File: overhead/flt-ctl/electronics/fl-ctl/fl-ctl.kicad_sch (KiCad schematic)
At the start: 29 parts, among them J1 Conn_02x01, J2 Conn_02x05_Counter_Clockwise

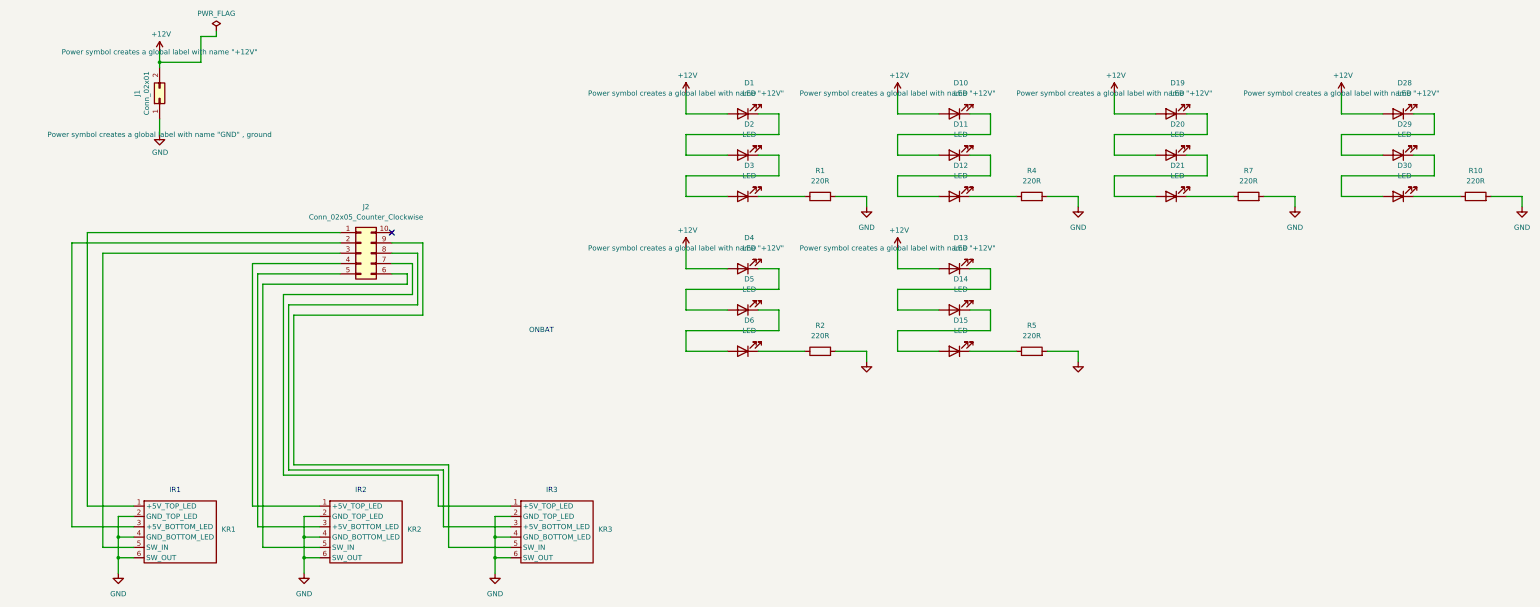
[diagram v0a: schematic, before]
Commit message: Finalised ROuting for FLT-CTL CPT Side, and cleaned up ADIRS Panel PCB
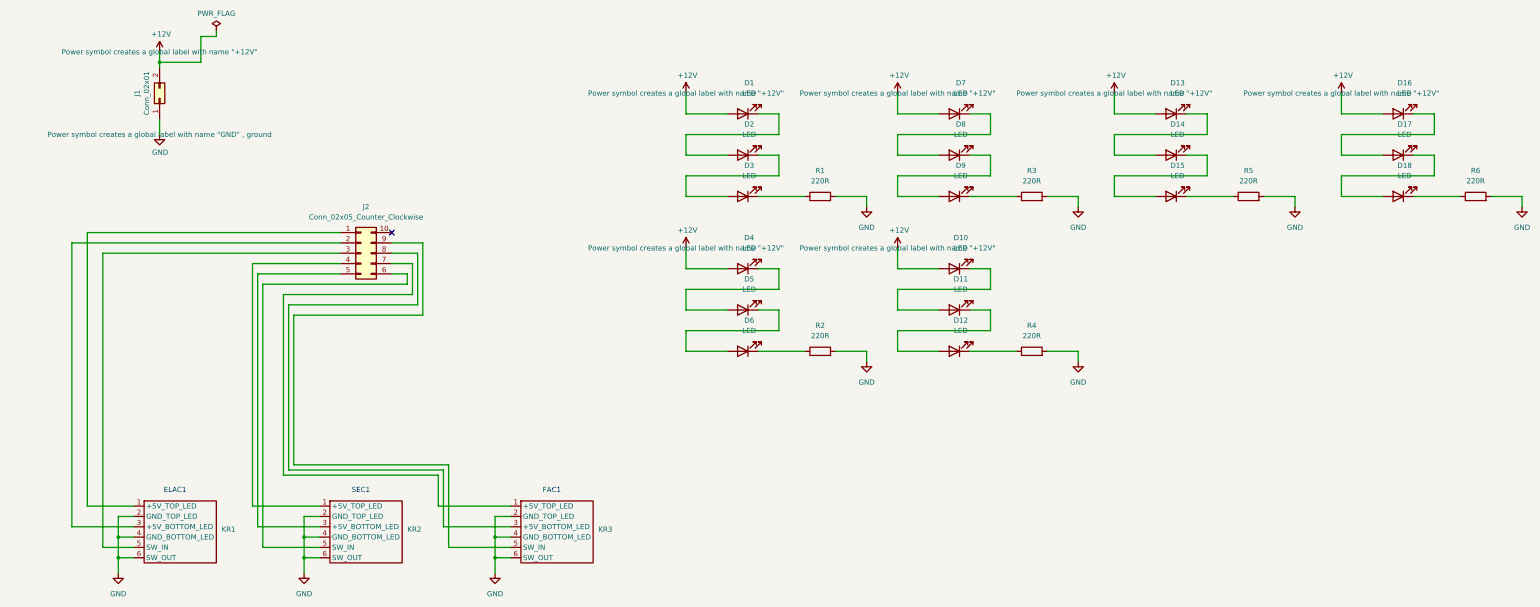
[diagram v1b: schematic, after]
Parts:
- renumbered D13 to D10, D14 to D11, D15 to D12, D19 to D13, D20 to D14, D21 to D15, D28 to D16, D29 to D17, D30 to D18, D10 to D7, D11 to D8, D12 to D9, R4 to R3, R5 to R4, R7 to R5, R10 to R6
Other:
- note added: "ELAC1"
- note added: "FAC1"
- note added: "SEC1"
- note removed: "IR1"
- note removed: "IR2"
- note removed: "IR3"
- note removed: "ONBAT"

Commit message: Updated all LEDs for SMD!
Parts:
- D1, D10, D11, D12, D13, D14, D15, D16, D17, D18, D2, D3, D4, D5, D6, D7, D8, D9: footprint LED_THT:LED_D5.0mm_Clear -> OpenA3XX:LED_Everlight-SMD3528_3.5x2.8mm_67-21ST
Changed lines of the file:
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@@
 			)
 		)
-		(property "Footprint" "LED_THT:LED_D5.0mm_Clear"
+		(property "Footprint" "OpenA3XX:LED_Everlight-SMD3528_3.5x2.8mm_67-21ST"
 			(at 187.96 90.17 0)
 			(effects
@@
 			)
 		)
-		(property "Footprint" "LED_THT:LED_D5.0mm_Clear"
+		(property "Footprint" "OpenA3XX:LED_Everlight-SMD3528_3.5x2.8mm_67-21ST"
 			(at 349.25 62.23 0)
 			(effects
@@
 			)
 		)
-		(property "Footprint" "LED_THT:LED_D5.0mm_Clear"
+		(property "Footprint" "OpenA3XX:LED_Everlight-SMD3528_3.5x2.8mm_67-21ST"
 			(at 187.96 100.33 0)
 			(effects
@@
 			)
 		)
-		(property "Footprint" "LED_THT:LED_D5.0mm_Clear"
+		(property "Footprint" "OpenA3XX:LED_Everlight-SMD3528_3.5x2.8mm_67-21ST"
 			(at 293.37 52.07 0)
 			(effects
@@
 			)
 		)
-		(property "Footprint" "LED_THT:LED_D5.0mm_Clear"
+		(property "Footprint" "OpenA3XX:LED_Everlight-SMD3528_3.5x2.8mm_67-21ST"
 			(at 349.25 52.07 0)
 			(effects
@@
 			)
 		)
-		(property "Footprint" "LED_THT:LED_D5.0mm_Clear"
+		(property "Footprint" "OpenA3XX:LED_Everlight-SMD3528_3.5x2.8mm_67-21ST"
 			(at 293.37 62.23 0)
 			(effects
@@
 			)
 		)
-		(property "Footprint" "LED_THT:LED_D5.0mm_Clear"
+		(property "Footprint" "OpenA3XX:LED_Everlight-SMD3528_3.5x2.8mm_67-21ST"
 			(at 240.03 41.91 0)
 			(effects
@@
 			)
 		)
-		(property "Footprint" "LED_THT:LED_D5.0mm_Clear"
+		(property "Footprint" "OpenA3XX:LED_Everlight-SMD3528_3.5x2.8mm_67-21ST"
 			(at 240.03 62.23 0)
 			(effects
@@
 			)
 		)
-		(property "Footprint" "LED_THT:LED_D5.0mm_Clear"
+		(property "Footprint" "OpenA3XX:LED_Everlight-SMD3528_3.5x2.8mm_67-21ST"
 			(at 349.25 41.91 0)
 			(effects
@@
 			)
 		)
-		(property "Footprint" "LED_THT:LED_D5.0mm_Clear"
+		(property "Footprint" "OpenA3XX:LED_Everlight-SMD3528_3.5x2.8mm_67-21ST"
 			(at 293.37 41.91 0)
 			(effects
@@
 			)
 		)
-		(property "Footprint" "LED_THT:LED_D5.0mm_Clear"
+		(property "Footprint" "OpenA3XX:LED_Everlight-SMD3528_3.5x2.8mm_67-21ST"
 			(at 187.96 41.91 0)
 			(effects
@@
 			)
 		)
-		(property "Footprint" "LED_THT:LED_D5.0mm_Clear"
+		(property "Footprint" "OpenA3XX:LED_Everlight-SMD3528_3.5x2.8mm_67-21ST"
 			(at 187.96 52.07 0)
 			(effects
@@
 			)
 		)
-		(property "Footprint" "LED_THT:LED_D5.0mm_Clear"
+		(property "Footprint" "OpenA3XX:LED_Everlight-SMD3528_3.5x2.8mm_67-21ST"
 			(at 187.96 80.01 0)
 			(effects
@@
 			)
 		)
-		(property "Footprint" "LED_THT:LED_D5.0mm_Clear"
+		(property "Footprint" "OpenA3XX:LED_Everlight-SMD3528_3.5x2.8mm_67-21ST"
 			(at 240.03 90.17 0)
 			(effects
@@
 			)
 		)
-		(property "Footprint" "LED_THT:LED_D5.0mm_Clear"
+		(property "Footprint" "OpenA3XX:LED_Everlight-SMD3528_3.5x2.8mm_67-21ST"
 			(at 240.03 100.33 0)
 			(effects
@@
 			)
 		)
-		(property "Footprint" "LED_THT:LED_D5.0mm_Clear"
+		(property "Footprint" "OpenA3XX:LED_Everlight-SMD3528_3.5x2.8mm_67-21ST"
 			(at 240.03 80.01 0)
 			(effects
@@
 			)
 		)
-		(property "Footprint" "LED_THT:LED_D5.0mm_Clear"
+		(property "Footprint" "OpenA3XX:LED_Everlight-SMD3528_3.5x2.8mm_67-21ST"
 			(at 187.96 62.23 0)
 			(effects
@@
 			)
 		)
-		(property "Footprint" "LED_THT:LED_D5.0mm_Clear"
+		(property "Footprint" "OpenA3XX:LED_Everlight-SMD3528_3.5x2.8mm_67-21ST"
 			(at 240.03 52.07 0)
 			(effects
